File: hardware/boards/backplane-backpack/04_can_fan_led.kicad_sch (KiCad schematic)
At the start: 22 parts, among them J2 CANH/CANL/GND (TBD), J9 12V FAN (TBD), Q1 AO3407A, Q2 2N7002,215, U3 TCAN3413DR

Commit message: chore: checkpoint workspace changes
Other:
- company: (none) -> Karl Quinsland
- title: CAN Fan and Status -> Backplane Backpack

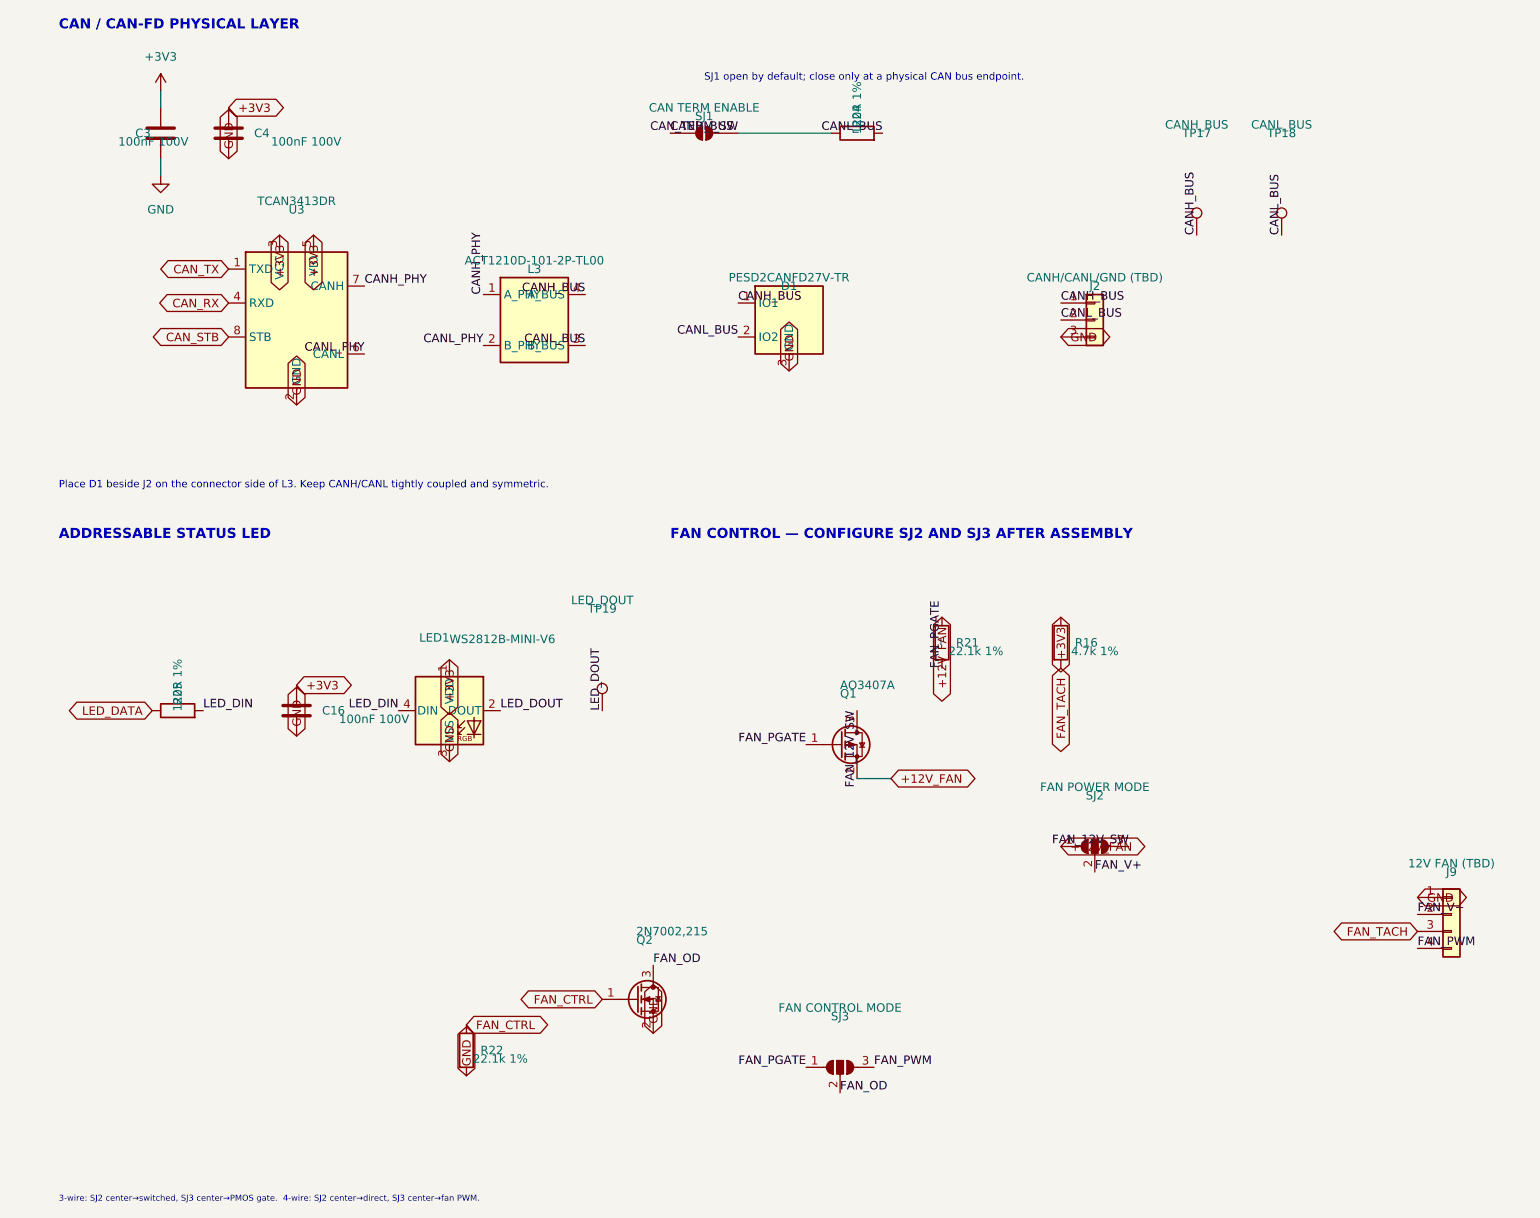
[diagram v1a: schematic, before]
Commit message: fix: normalize power symbols and connector grounds
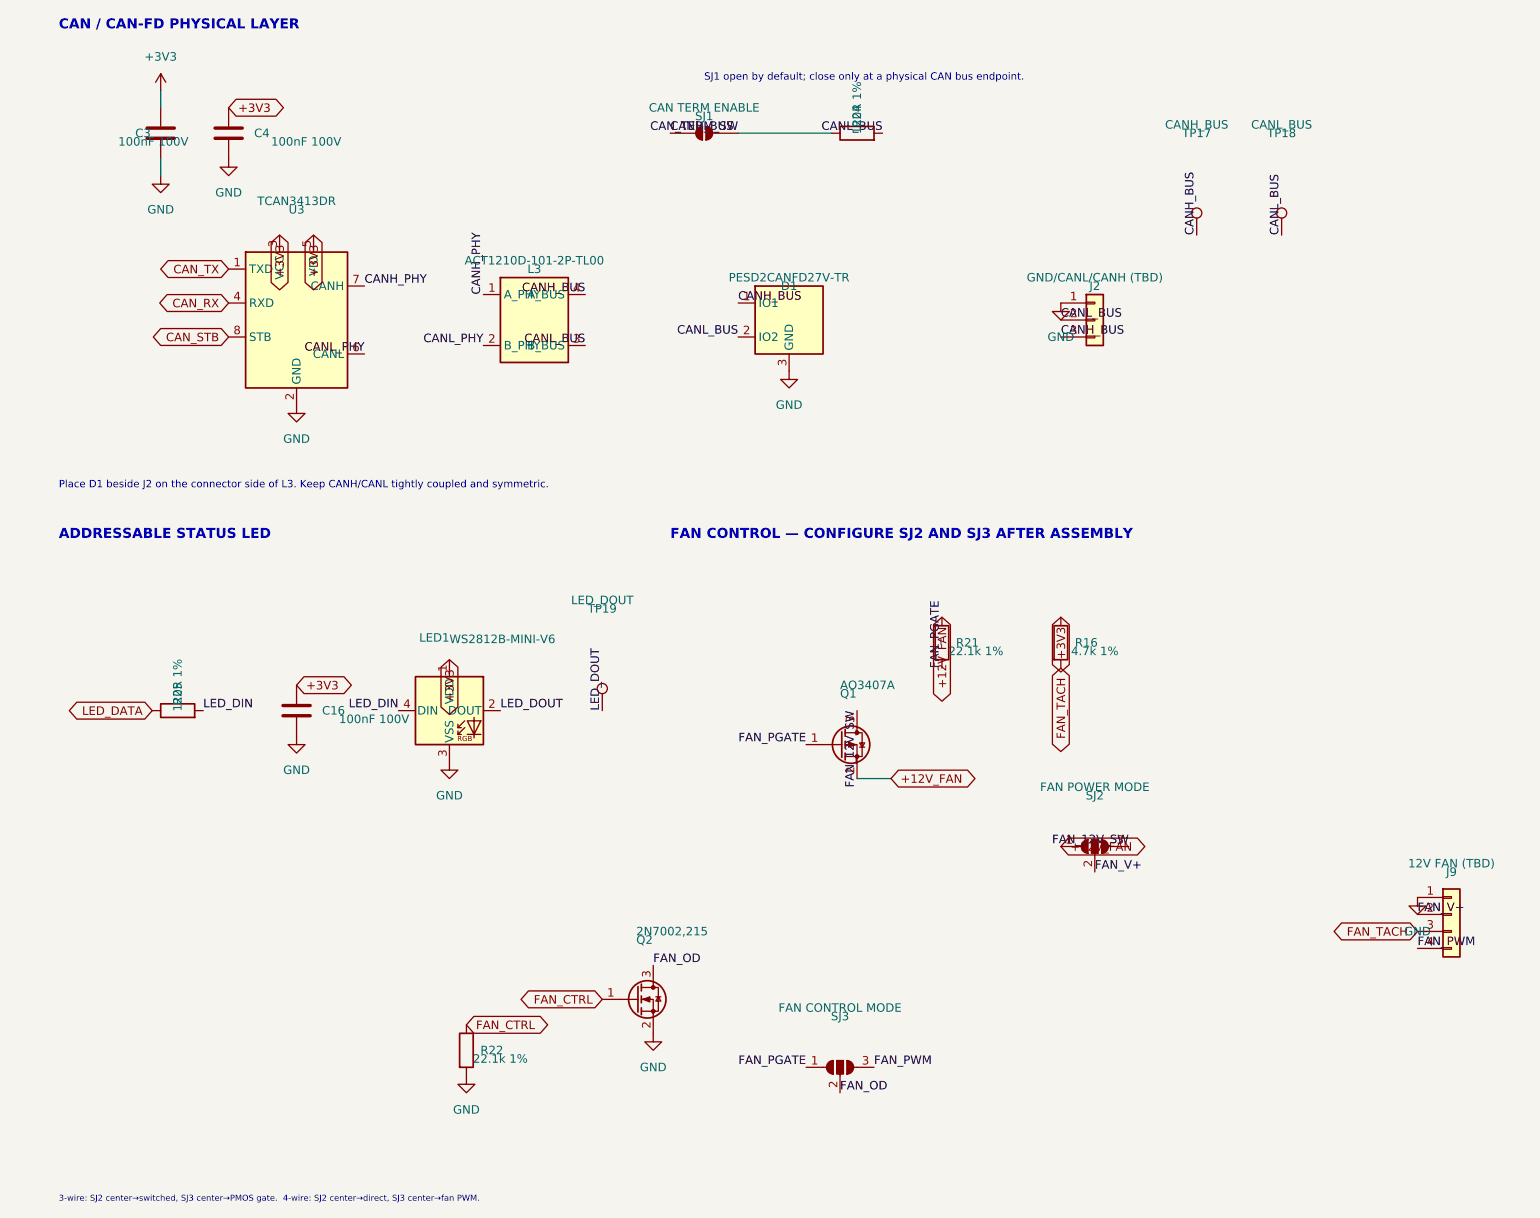
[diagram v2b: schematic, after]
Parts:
- J2: value CANH/CANL/GND (TBD) -> GND/CANL/CANH (TBD)
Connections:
- net CANH_BUS: now also J2.3 (Pin_3); no longer J2.1 (Pin_1)
- net GND: now also J2.1 (Pin_1); no longer J2.3 (Pin_3)

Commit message: fix: standardize +3V3 power symbols
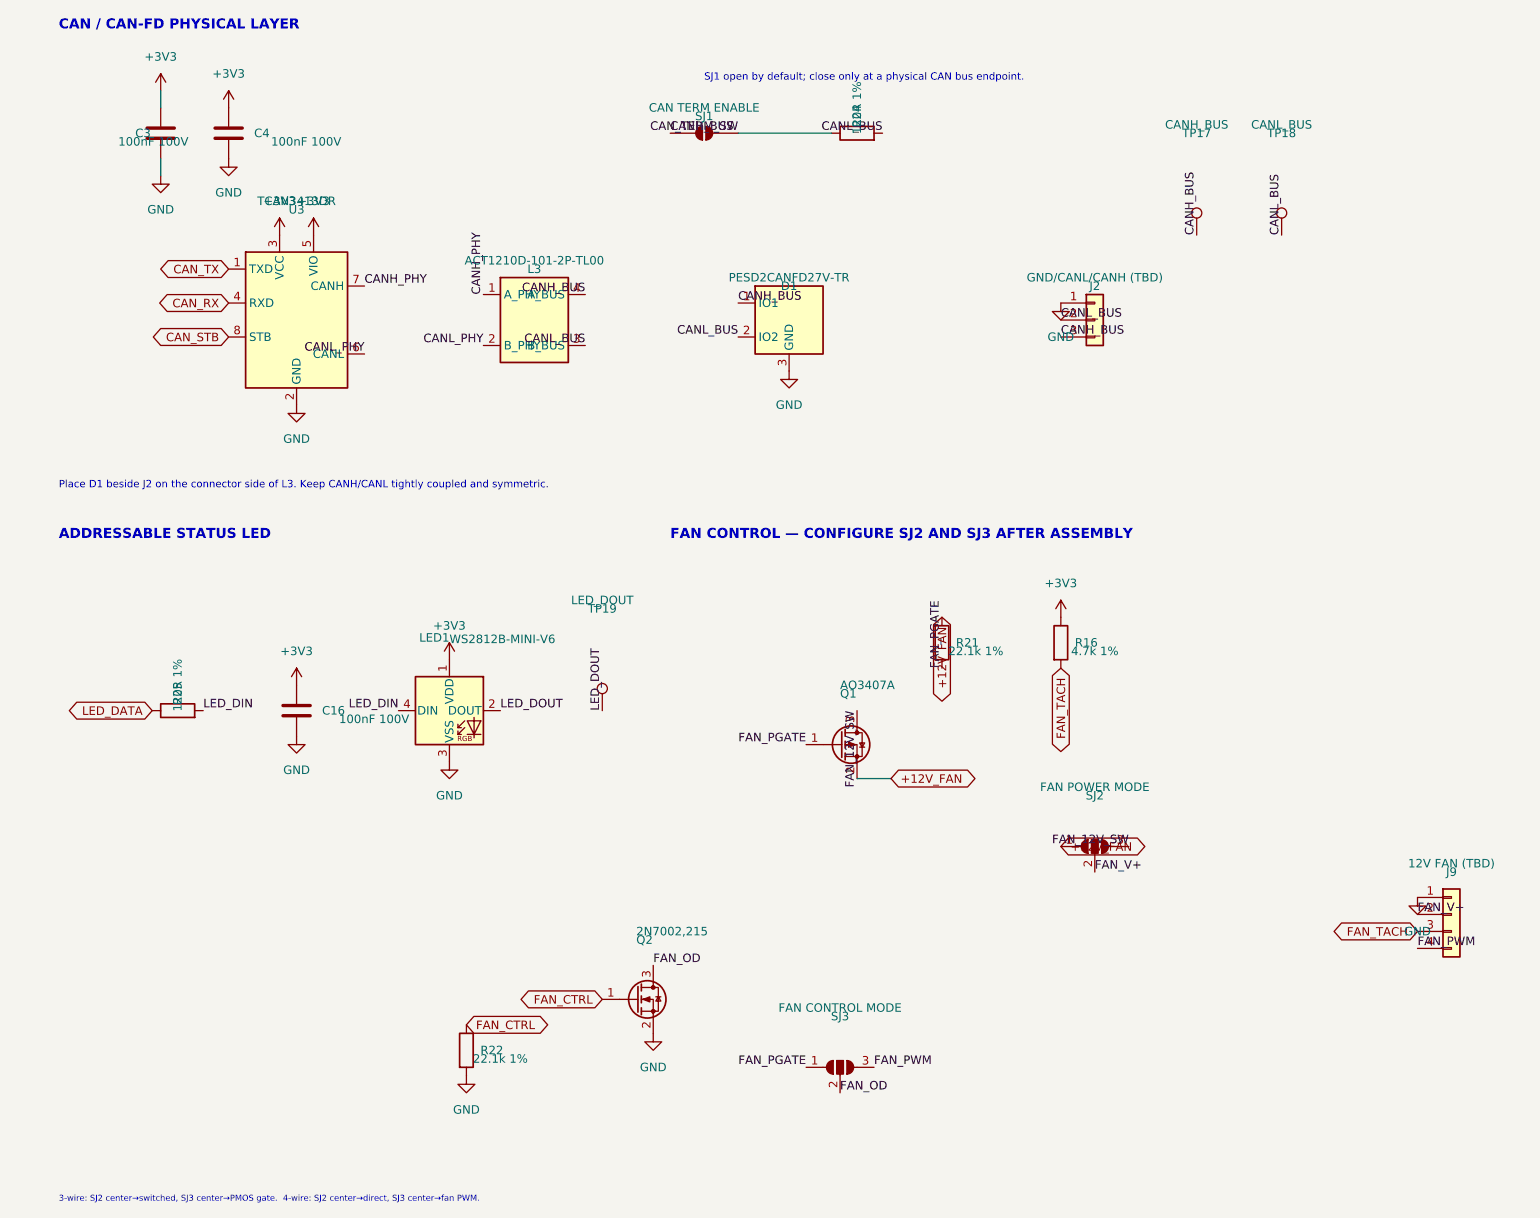
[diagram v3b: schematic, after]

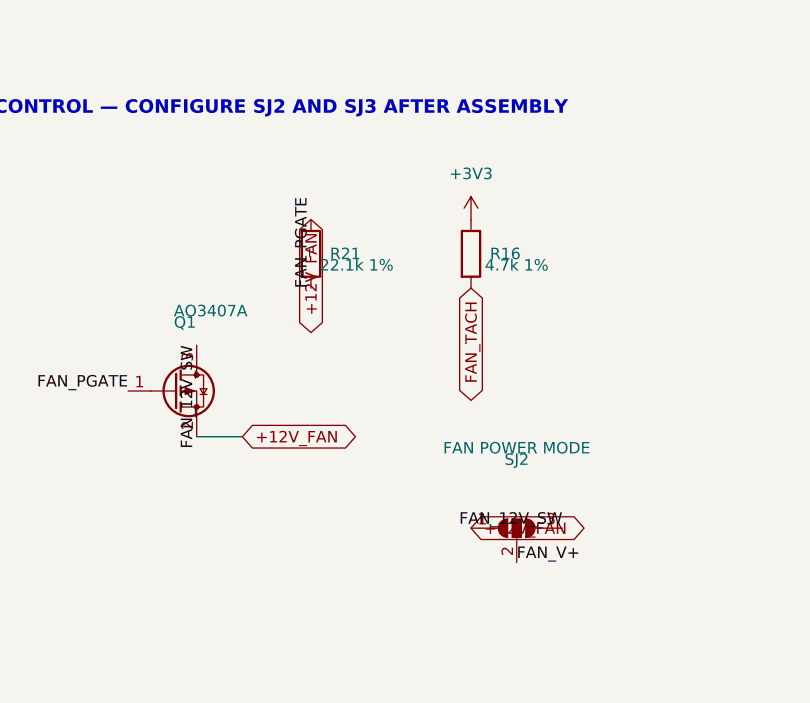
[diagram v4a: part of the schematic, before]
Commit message: fix: standardize 12V rail and mirror buck layout
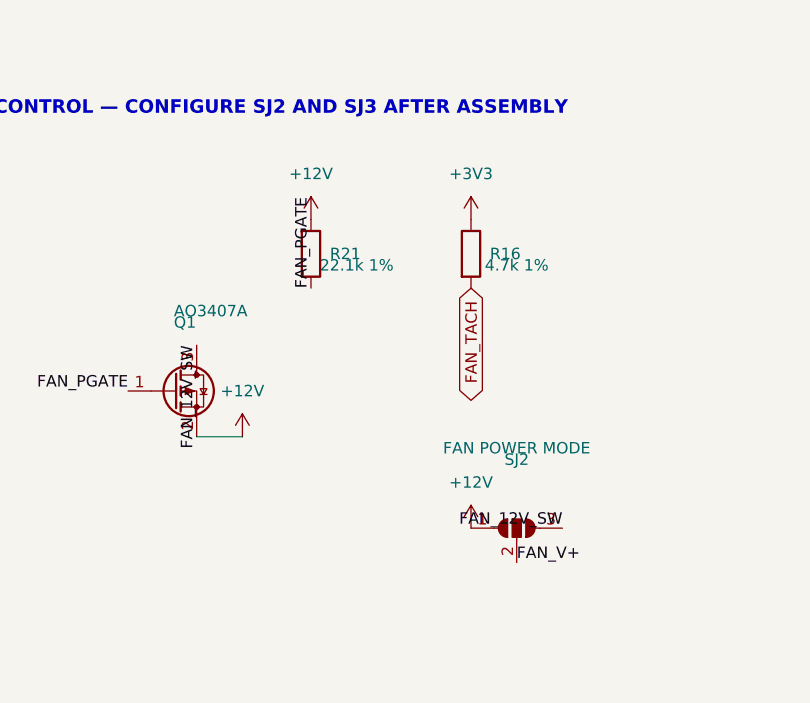
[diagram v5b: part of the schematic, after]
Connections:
- net +12V_FAN renamed +12V
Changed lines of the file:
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@@
 		)
 	)
-	(global_label "+12V_FAN"
-		(shape bidirectional)
+	(symbol
+		(lib_id "power:+12V")
 		(at 170.18 137.16 0)
-		(effects
-			(font
-				(size 1.27 1.27)
-			)
-			(justify left bottom)
-		)
-		(property "Intersheetrefs" "${INTERSHEET_REFS}"
+		(unit 1)
+		(body_style 1)
+		(exclude_from_sim no)
+		(in_bom yes)
+		(on_board yes)
+		(in_pos_files yes)
+		(dnp no)
+		(fields_autoplaced yes)
+		(property "Reference" "#PWR0418"
+			(at 170.18 140.97 0)
+			(hide yes)
+			(show_name no)
+			(do_not_autoplace no)
+			(effects
+				(font
+					(size 1.27 1.27)
+				)
+			)
+		)
+		(property "Value" "+12V"
+			(at 170.18 132.08 0)
+			(show_name no)
+			(do_not_autoplace no)
+			(effects
+				(font
+					(size 1.27 1.27)
+				)
+			)
+		)
+		(property "Footprint" ""
 			(at 170.18 137.16 0)
 			(hide yes)
@@
 				(font
 					(size 1.27 1.27)
+				)
+			)
+		)
+		(property "Datasheet" ""
+			(at 170.18 137.16 0)
+			(hide yes)
+			(show_name no)
+			(do_not_autoplace no)
+			(effects
+				(font
+					(size 1.27 1.27)
+				)
+			)
+		)
+		(property "Description" "Power symbol creates a global label with name \"+12V\""
+			(at 170.18 137.16 0)
+			(hide yes)
+			(show_name no)
+			(do_not_autoplace no)
+			(effects
+				(font
+					(size 1.27 1.27)
+				)
+			)
+		)
+		(pin "1"
+		)
+		(instances
+			(project "backplane-backpack"
+				(path "/76314aad-fff2-4237-8c4a-2dbd4e06a2e1/ca945800-30c4-4174-8f18-f8602dd80706"
+					(reference "#PWR0418")
+					(unit 1)
 				)
 			)
@@
 		)
 	)
-	(global_label "+12V_FAN"
-		(shape bidirectional)
+	(symbol
+		(lib_id "power:+12V")
 		(at 144.78 127 0)
-		(effects
-			(font
-				(size 1.27 1.27)
-			)
-			(justify left)
-		)
-		(property "Intersheetrefs" "${INTERSHEET_REFS}"
+		(unit 1)
+		(body_style 1)
+		(exclude_from_sim no)
+		(in_bom yes)
+		(on_board yes)
+		(in_pos_files yes)
+		(dnp no)
+		(fields_autoplaced yes)
+		(property "Reference" "#PWR0419"
+			(at 144.78 130.81 0)
+			(hide yes)
+			(show_name no)
+			(do_not_autoplace no)
+			(effects
+				(font
+					(size 1.27 1.27)
+				)
+			)
+		)
+		(property "Value" "+12V"
+			(at 144.78 121.92 0)
+			(show_name no)
+			(do_not_autoplace no)
+			(effects
+				(font
+					(size 1.27 1.27)
+				)
+			)
+		)
+		(property "Footprint" ""
 			(at 144.78 127 0)
 			(hide yes)
@@
 				(font
 					(size 1.27 1.27)
+				)
+			)
+		)
+		(property "Datasheet" ""
+			(at 144.78 127 0)
+			(hide yes)
+			(show_name no)
+			(do_not_autoplace no)
+			(effects
+				(font
+					(size 1.27 1.27)
+				)
+			)
+		)
+		(property "Description" "Power symbol creates a global label with name \"+12V\""
+			(at 144.78 127 0)
+			(hide yes)
+			(show_name no)
+			(do_not_autoplace no)
+			(effects
+				(font
+					(size 1.27 1.27)
+				)
+			)
+		)
+		(pin "1"
+		)
+		(instances
+			(project "backplane-backpack"
+				(path "/76314aad-fff2-4237-8c4a-2dbd4e06a2e1/ca945800-30c4-4174-8f18-f8602dd80706"
+					(reference "#PWR0419")
+					(unit 1)
 				)
 			)
@@
 		)
 	)
-	(global_label "+12V_FAN"
-		(shape bidirectional)
-		(at 152.4 102.87 270)
-		(effects
-			(font
-				(size 1.27 1.27)
-			)
-			(justify right bottom)
-		)
-		(property "Intersheetrefs" "${INTERSHEET_REFS}"
+	(symbol
+		(lib_id "power:+12V")
+		(at 152.4 102.87 0)
+		(unit 1)
+		(body_style 1)
+		(exclude_from_sim no)
+		(in_bom yes)
+		(on_board yes)
+		(in_pos_files yes)
+		(dnp no)
+		(fields_autoplaced yes)
+		(property "Reference" "#PWR0420"
+			(at 152.4 106.68 0)
+			(hide yes)
+			(show_name no)
+			(do_not_autoplace no)
+			(effects
+				(font
+					(size 1.27 1.27)
+				)
+			)
+		)
+		(property "Value" "+12V"
+			(at 152.4 97.79 0)
+			(show_name no)
+			(do_not_autoplace no)
+			(effects
+				(font
+					(size 1.27 1.27)
+				)
+			)
+		)
+		(property "Footprint" ""
 			(at 152.4 102.87 0)
 			(hide yes)
@@
 				)
 			)
+		)
+		(property "Datasheet" ""
+			(at 152.4 102.87 0)
+			(hide yes)
+			(show_name no)
+			(do_not_autoplace no)
+			(effects
+				(font
+					(size 1.27 1.27)
+				)
+			)
+		)
+		(property "Description" "Power symbol creates a global label with name \"+12V\""
+			(at 152.4 102.87 0)
+			(hide yes)
+			(show_name no)
+			(do_not_autoplace no)
+			(effects
+				(font
+					(size 1.27 1.27)
+				)
+			)
+		)
+		(pin "1"
+		)
+		(instances
+			(project "backplane-backpack"
+				(path "/76314aad-fff2-4237-8c4a-2dbd4e06a2e1/ca945800-30c4-4174-8f18-f8602dd80706"
+					(reference "#PWR0420")
+					(unit 1)
+				)
+			)

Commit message: chore: checkpoint current board layout
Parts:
- removed C16: 100nF 100V, Capacitor_SMD:C_0603_1608Metric, symbol Device:C
- removed R25: 120R 1%, Resistor_SMD:R_0603_1608Metric, symbol Device:R
- added TP10: FAN_TACH, TestPoint:TestPoint_Pad_D1.5mm, symbol Connector:TestPoint
- added TP11: LED_DATA, TestPoint:TestPoint_Pad_D1.5mm, symbol Connector:TestPoint
- added TP5: CAN_TX, TestPoint:TestPoint_Pad_D1.5mm, symbol Connector:TestPoint
- added TP6: CAN_RX, TestPoint:TestPoint_Pad_D1.5mm, symbol Connector:TestPoint
- added TP9: FAN_CTRL, TestPoint:TestPoint_Pad_D1.5mm, symbol Connector:TestPoint
- J9: value 12V FAN (TBD) -> 12V FAN
- R24: now not fitted
- SJ1: value CAN TERM ENABLE -> CAN TERMINATE
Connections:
- net LED_DIN is gone; now on net LED_DATA: LED1.4 (DIN)
- net CAN_RX: now also TP6.1
- net CAN_TX: now also TP5.1
- net FAN_CTRL: now also TP9.1
- net FAN_TACH: now also TP10.1
- net LED_DATA: now also TP11.1
- net CAN_TERM_SW: no longer names the net of R24.1, SJ1.2 (B)
- net FAN_OD: no longer names the net of Q2.3 (D), SJ3.2 (C)
- net FAN_PGATE: no longer names the net of Q1.1 (G), R21.2, SJ3.1 (A)
- net FAN_V+: no longer names the net of J9.2 (Pin_2), SJ2.2 (C)
- net LED_DOUT: no longer names the net of LED1.2 (DOUT), TP19.1
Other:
- note added: "Open by default, DNP the resistor"
- note added: "Support 3 or 4 wire configuration. 3-wire: SJ2 center→switched, SJ3 center→PMOS gate. 4-wire: SJ2 center→direct, SJ3 center→fan PWM."
- note removed: "3-wire: SJ2 center→switched, SJ3 center→PMOS gate. 4-wire: SJ2 center→direct, SJ3 center→fan PWM."
- note removed: "SJ1 open by default; close only at a physical CAN bus endpoint."
- moved on the sheet: C3, C4, D1, J2, J9, L3, LED1, Q1, Q2, R16, R22, SJ2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
